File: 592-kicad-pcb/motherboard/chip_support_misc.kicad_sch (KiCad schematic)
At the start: 9 parts, among them J6 2.54mm jumper, J7 Conn_01x01, SW1 C318884, U6 74LVC1T45GW, U7 NC7SVU04P5X

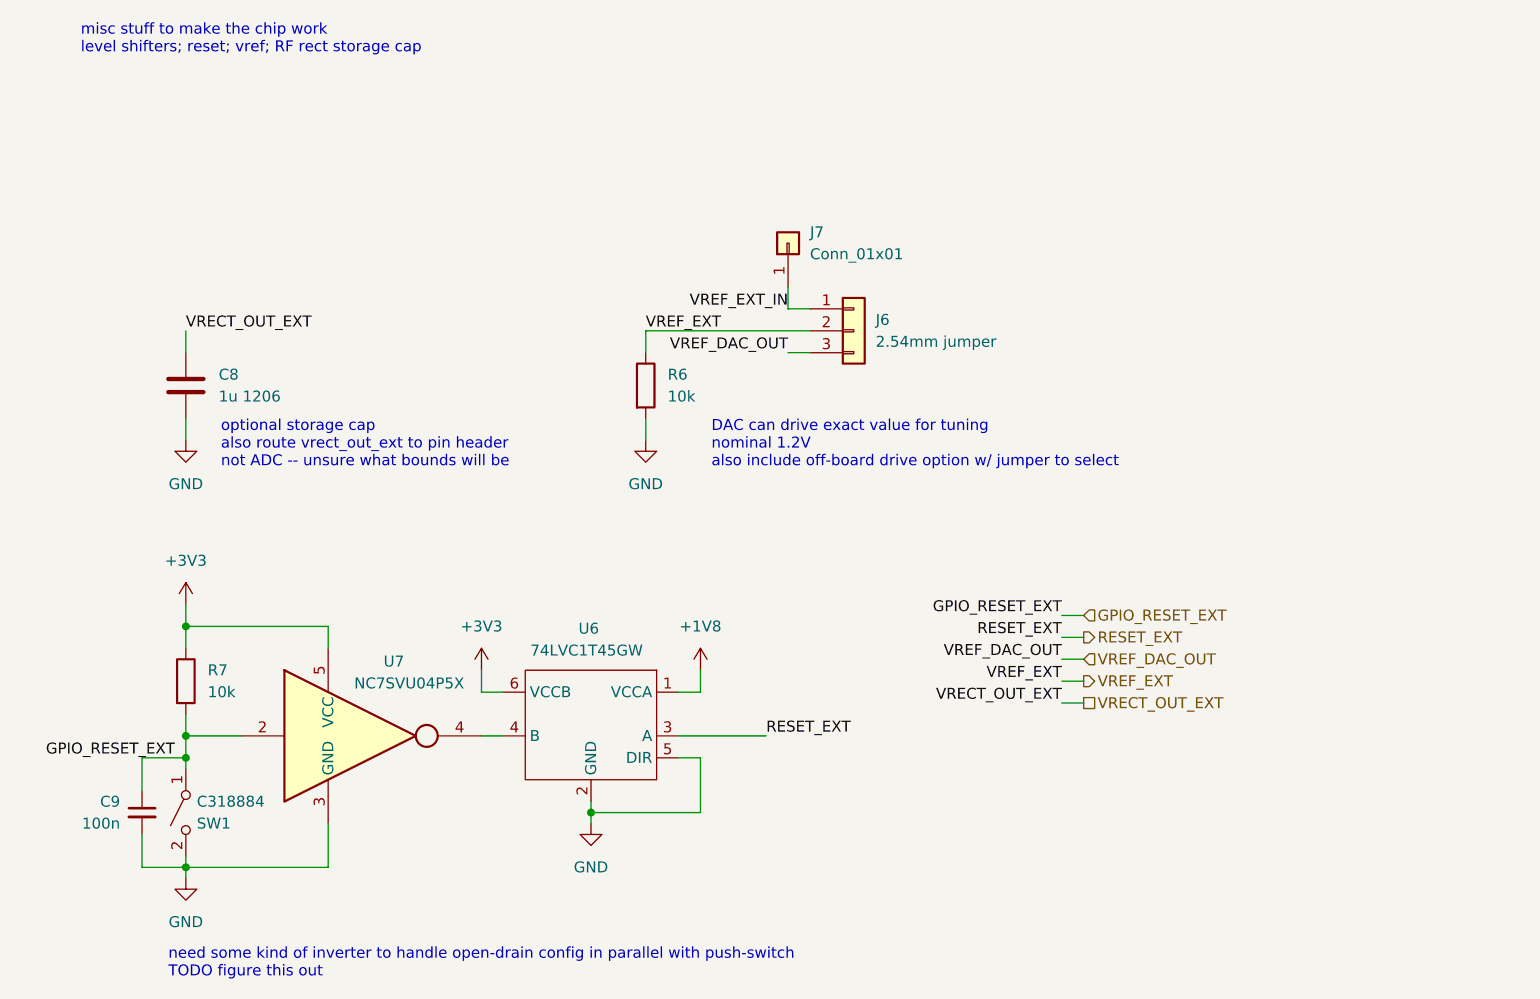
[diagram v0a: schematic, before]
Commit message: clean up supporting blocks; add nucleo symbol
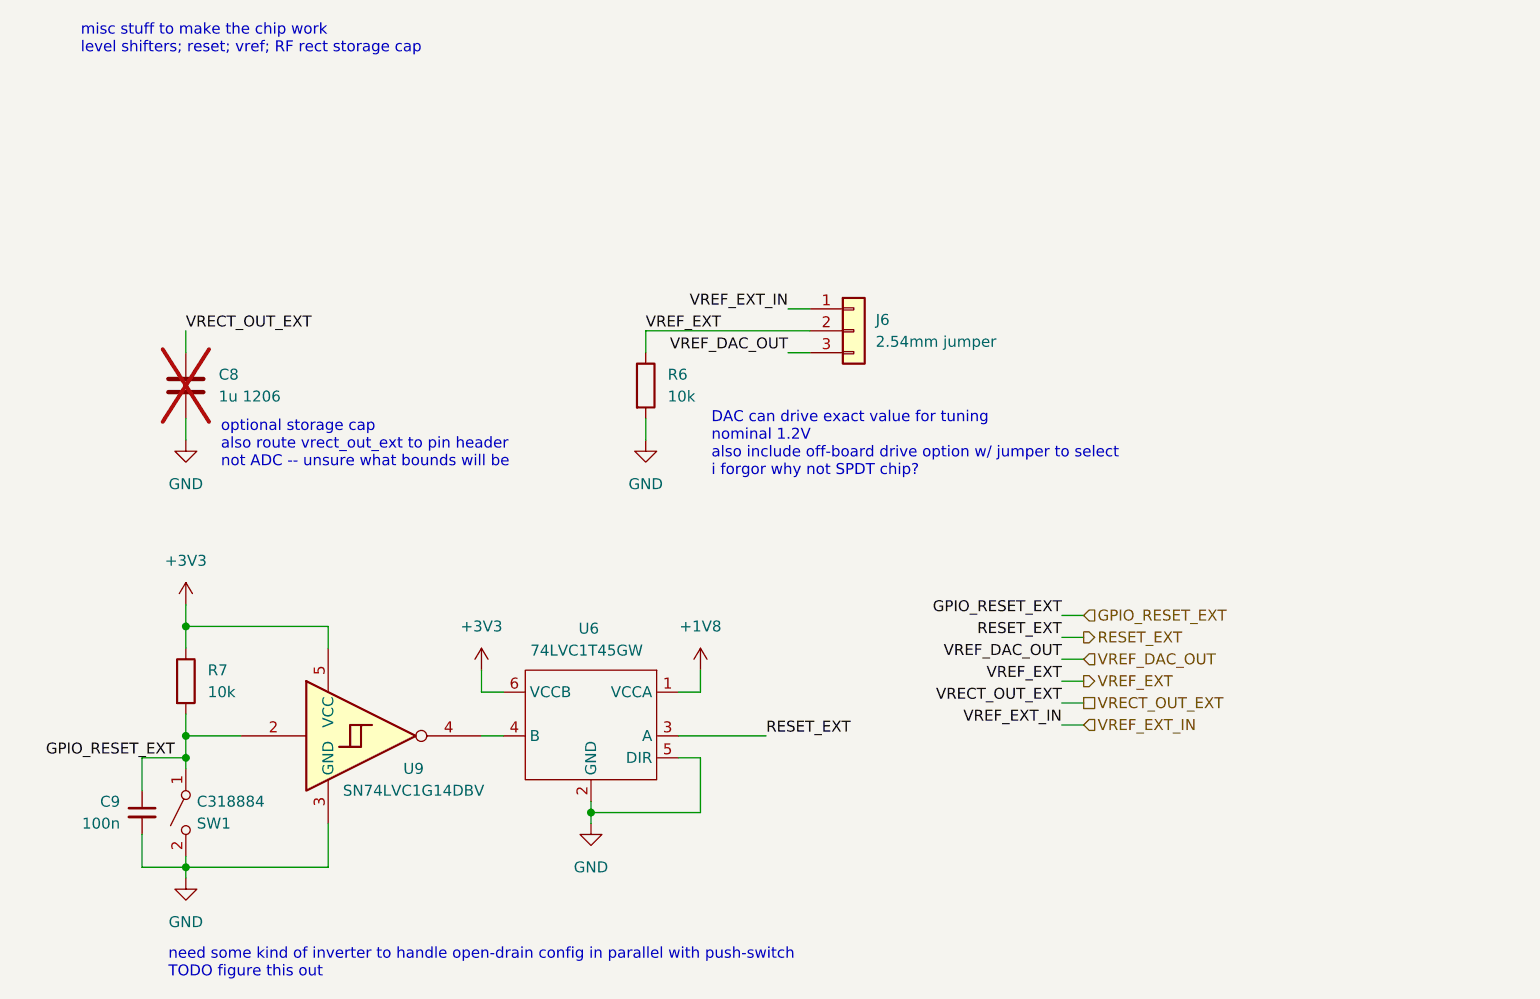
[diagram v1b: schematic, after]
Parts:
- removed J7: Conn_01x01, symbol Connector_Generic:Conn_01x01
- removed U7: NC7SVU04P5X, Package_TO_SOT_SMD:SOT-353_SC-70-5, symbol 74xGxx:NC7SVU04P5X
- added U9: SN74LVC1G14DBV, Package_TO_SOT_SMD:SOT-23-5, symbol 74xGxx:SN74LVC1G14DBV
- C8: now not fitted
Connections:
- net +3V3: now also U9.5 (VCC)
- net GND: now also U9.3 (GND)
- net GPIO_RESET_EXT: now also U9.2
- net at U6.4 (B): now also U9.4
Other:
- note added: "DAC can drive exact value for tuning nominal 1.2V also include off-board drive option w/ jumper to select i forgor why not SPDT chip?"
- note removed: "DAC can drive exact value for tuning nominal 1.2V also include off-board drive option w/ jumper to select"
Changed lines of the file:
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@@
 		)
 	)
-	(text "DAC can drive exact value for tuning\nnominal 1.2V\nalso include off-board drive option w/ jumper to select"
+	(text "DAC can drive exact value for tuning\nnominal 1.2V\nalso include off-board drive option w/ jumper to select\ni forgor why not SPDT chip?"
 		(exclude_from_sim no)
 		(at 95.25 67.818 0)
@@
 	(wire
 		(pts
+			(xy 135.89 100.33) (xy 138.43 100.33)
+		)
+		(stroke
+			(width 0)
+			(type default)
+		)
+	)
+	(wire
+		(pts
 			(xy 68.58 93.98) (xy 68.58 96.52)
 		)
@@
 		(pts
 			(xy 34.29 101.6) (xy 34.29 104.14)
-		)
-		(stroke
-			(width 0)
-			(type default)
-		)
-	)
-	(wire
-		(pts
-			(xy 104.14 49.53) (xy 104.14 52.07)
 		)
 		(stroke
@@
 		)
 	)
+	(label "VREF_EXT_IN"
+		(at 135.89 100.33 180)
+		(effects
+			(font
+				(size 1.27 1.27)
+			)
+			(justify right bottom)
+		)
+	)
 	(label "VREF_DAC_OUT"
 		(at 135.89 92.71 180)
@@
 			)
 			(justify right bottom)
+		)
+	)
+	(hierarchical_label "VREF_EXT_IN"
+		(shape input)
+		(at 138.43 100.33 0)
+		(effects
+			(font
+				(size 1.27 1.27)
+			)
+			(justify left)
 		)
 	)
@@
 				(path "/5b0c97ac-fa03-4db8-b41b-0eee32b6f55d/1be5e80d-5a74-4ad9-b42f-508050f3350a"
 					(reference "C9")
+					(unit 1)
+				)
+			)
+		)
+	)
+	(symbol
+		(lib_id "74xGxx:SN74LVC1G14DBV")
+		(at 55.88 101.6 0)
+		(unit 1)
+		(exclude_from_sim no)
+		(in_bom yes)
+		(on_board yes)
+		(dnp no)
+		(property "Reference" "U9"
+			(at 60.706 105.41 0)
+			(effects
+				(font
+					(size 1.27 1.27)
+				)
+			)
+		)
+		(property "Value" "SN74LVC1G14DBV"
+			(at 60.706 107.95 0)
+			(effects
+				(font
+					(size 1.27 1.27)
+				)
+			)
+		)
+		(property "Footprint" "Package_TO_SOT_SMD:SOT-23-5"
+			(at 55.88 107.95 0)
+			(effects
+				(font
+					(size 1.27 1.27)
+					(italic yes)
+				)
+				(justify left)
+				(hide yes)
+			)
+		)
+		(property "Datasheet" "https://www.ti.com/lit/ds/symlink/sn74lvc1g14.pdf"
+			(at 55.88 110.49 0)
+			(effects
+				(font
+					(size 1.27 1.27)
+				)
+				(justify left)
+				(hide yes)
+			)
+		)
+		(property "Description" "Single Schmitt NOT Gate, Low-Voltage CMOS, SOT-23"
+			(at 55.88 101.6 0)
+			(effects
+				(font
+					(size 1.27 1.27)
+				)
+				(hide yes)
+			)
+		)
+		(pin "4"
+		)
+		(pin "2"
+		)
+		(pin "1"
+		)
+		(pin "5"
+		)
+		(pin "3"
+		)
+		(instances
+			(project ""
+				(path "/5b0c97ac-fa03-4db8-b41b-0eee32b6f55d/1be5e80d-5a74-4ad9-b42f-508050f3350a"
+					(reference "U9")
 					(unit 1)
 				)
@@
 	)
 	(symbol
-		(lib_id "74xGxx:NC7SVU04P5X")
-		(at 50.8 101.6 0)
-		(unit 1)
-		(exclude_from_sim no)
-		(in_bom yes)
-		(on_board yes)
-		(dnp no)
-		(property "Reference" "U7"
-			(at 58.42 92.964 0)
-			(effects
-				(font
-					(size 1.27 1.27)
-				)
-			)
-		)
-		(property "Value" "NC7SVU04P5X"
-			(at 60.198 95.504 0)
-			(effects
-				(font
-					(size 1.27 1.27)
-				)
-			)
-		)
-		(property "Footprint" "Package_TO_SOT_SMD:SOT-353_SC-70-5"
-			(at 50.8 114.3 0)
-			(effects
-				(font
-					(size 1.27 1.27)
-				)
-				(hide yes)
-			)
-		)
-		(property "Datasheet" "https://www.onsemi.com/pub/Collateral/NC7SVU04-D.pdf"
-			(at 50.8 101.6 0)
-			(effects
-				(font
-					(size 1.27 1.27)
-				)
-				(hide yes)
-			)
-		)
-		(property "Description" "High-Speed Logic Inverter, SOT-353"
-			(at 50.8 101.6 0)
-			(effects
-				(font
-					(size 1.27 1.27)
-				)
-				(hide yes)
-			)
-		)
-		(pin "3"
-		)
-		(pin "5"
-		)
-		(pin "2"
-		)
-		(pin "1"
-		)
-		(pin "4"
-		)
-		(instances
-			(project ""
-				(path "/5b0c97ac-fa03-4db8-b41b-0eee32b6f55d/1be5e80d-5a74-4ad9-b42f-508050f3350a"
-					(reference "U7")
-					(unit 1)
-				)
-			)
-		)
-	)
-	(symbol
 		(lib_id "Device:C")
 		(at 34.29 60.96 0)
@@
 		(in_bom yes)
 		(on_board yes)
-		(dnp no)
+		(dnp yes)
 		(fields_autoplaced yes)
 		(property "Reference" "C8"
@@
 	)
 	(symbol
-		(lib_id "Connector_Generic:Conn_01x01")
-		(at 104.14 44.45 90)
-		(unit 1)
-		(exclude_from_sim no)
-		(in_bom yes)
-		(on_board yes)
-		(dnp no)
-		(fields_autoplaced yes)
-		(property "Reference" "J7"
-			(at 106.68 43.1799 90)
-			(effects
-				(font
-					(size 1.27 1.27)
-				)
-				(justify right)
-			)
-		)
-		(property "Value" "Conn_01x01"
-			(at 106.68 45.7199 90)
-			(effects
-				(font
-					(size 1.27 1.27)
-				)
-				(justify right)
-			)
-		)
-		(property "Footprint" ""
-			(at 104.14 44.45 0)
-			(effects
-				(font
-					(size 1.27 1.27)
-				)
-				(hide yes)
-			)
-		)
-		(property "Datasheet" "~"
-			(at 104.14 44.45 0)
-			(effects
-				(font
-					(size 1.27 1.27)
-				)
-				(hide yes)
-			)
-		)
-		(property "Description" "Generic connector, single row, 01x01, script generated (kicad-library-utils/schlib/autogen/connector/)"
-			(at 104.14 44.45 0)
-			(effects
-				(font
-					(size 1.27 1.27)
-				)
-				(hide yes)
-			)
-		)
-		(pin "1"
-		)
-		(instances
-			(project ""
-				(path "/5b0c97ac-fa03-4db8-b41b-0eee32b6f55d/1be5e80d-5a74-4ad9-b42f-508050f3350a"
-					(reference "J7")
-					(unit 1)
-				)
-			)
-		)
-	)
-	(symbol
 		(lib_id "power:+1V8")
 		(at 93.98 93.98 0)
@@
 			)
 		)
-		(property "Datasheet" ""
+		(property "Datasheet" "https://www.lcsc.com/datasheet/C478004.pdf"
 			(at 81.28 100.33 0)
 			(effects

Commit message: add footprints for signal conditioning
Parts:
- C8, C9, R6, R7: footprint (none) -> Capacitor_SMD:C_0603_1608Metric
- J6: footprint (none) -> Connector_PinHeader_2.54mm:PinHeader_1x03_P2.54mm_Vertical
- SW1: footprint (none) -> Button_Switch_SMD:SW_Push_1P1T_XKB_TS-1187A
- U6: footprint (none) -> Package_TO_SOT_SMD:SOT-363_SC-70-6
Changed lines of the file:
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@@
 			)
 		)
-		(property "Footprint" ""
+		(property "Footprint" "Capacitor_SMD:C_0603_1608Metric"
 			(at 29.21 110.49 0)
 			(effects
@@
 			)
 		)
-		(property "Footprint" ""
+		(property "Footprint" "Capacitor_SMD:C_0603_1608Metric"
 			(at 35.2552 64.77 0)
 			(effects
@@
 			)
 		)
-		(property "Footprint" ""
+		(property "Footprint" "Connector_PinHeader_2.54mm:PinHeader_1x03_P2.54mm_Vertical"
 			(at 111.76 54.61 0)
 			(effects
@@
 			)
 		)
-		(property "Footprint" ""
+		(property "Footprint" "Button_Switch_SMD:SW_Push_1P1T_XKB_TS-1187A"
 			(at 34.29 110.49 0)
 			(effects
@@
 			)
 		)
-		(property "Footprint" ""
+		(property "Footprint" "Capacitor_SMD:C_0603_1608Metric"
 			(at 32.512 95.25 90)
 			(effects
@@
 			)
 		)
-		(property "Footprint" ""
+		(property "Footprint" "Package_TO_SOT_SMD:SOT-363_SC-70-6"
 			(at 81.28 100.33 0)
 			(effects
@@
 			)
 		)
-		(property "Footprint" ""
+		(property "Footprint" "Capacitor_SMD:C_0603_1608Metric"
 			(at 85.852 60.96 90)
 			(effects

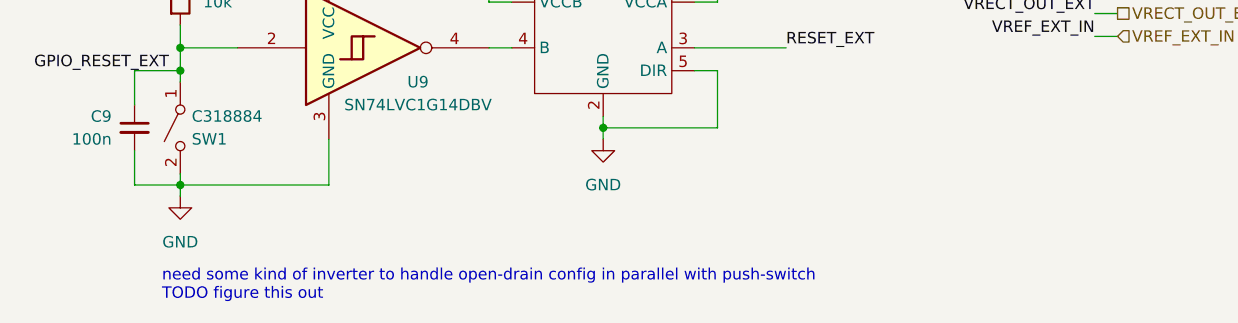
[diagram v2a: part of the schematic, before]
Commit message: update motheboard schems to include conn
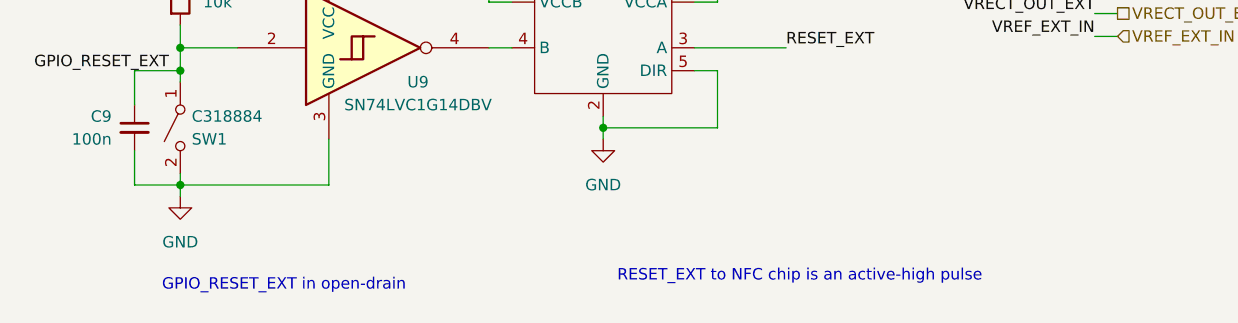
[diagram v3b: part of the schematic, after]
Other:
- note added: "GPIO_RESET_EXT in open-drain"
- note added: "RESET_EXT to NFC chip is an active-high pulse"
- note removed: "need some kind of inverter to handle open-drain config in parallel with push-switch TODO figure this out"
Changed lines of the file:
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@@
 	(generator_version "9.0")
 	(paper "A4")
-	(text "need some kind of inverter to handle open-drain config in parallel with push-switch\nTODO figure this out"
+	(text "GPIO_RESET_EXT in open-drain"
 		(exclude_from_sim no)
 		(at 32.258 128.016 0)
@@
 		)
 	)
+	(text "RESET_EXT to NFC chip is an active-high pulse"
+		(exclude_from_sim no)
+		(at 103.124 127 0)
+		(effects
+			(font
+				(size 1.27 1.27)
+			)
+		)
+	)

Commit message: add jlc stackup, size pulldowns
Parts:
- C8: footprint Capacitor_SMD:C_0603_1608Metric -> Resistor_SMD:R_1206_3216Metric
- R6, R7: footprint Capacitor_SMD:C_0603_1608Metric -> Resistor_SMD:R_0603_1608Metric
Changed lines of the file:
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@@
 			)
 		)
-		(property "Footprint" "Capacitor_SMD:C_0603_1608Metric"
+		(property "Footprint" "Resistor_SMD:R_1206_3216Metric"
 			(at 35.2552 64.77 0)
 			(effects
@@
 			)
 		)
-		(property "Footprint" "Capacitor_SMD:C_0603_1608Metric"
+		(property "Footprint" "Resistor_SMD:R_0603_1608Metric"
 			(at 32.512 95.25 90)
 			(effects
@@
 			)
 		)
-		(property "Footprint" "Capacitor_SMD:C_0603_1608Metric"
+		(property "Footprint" "Resistor_SMD:R_0603_1608Metric"
 			(at 85.852 60.96 90)
 			(effects
